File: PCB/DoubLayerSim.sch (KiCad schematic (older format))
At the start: 26 parts, among them J1 PanelSolar, J2 Bateria 3.7v, Q1 2N3904, U1 Moisture

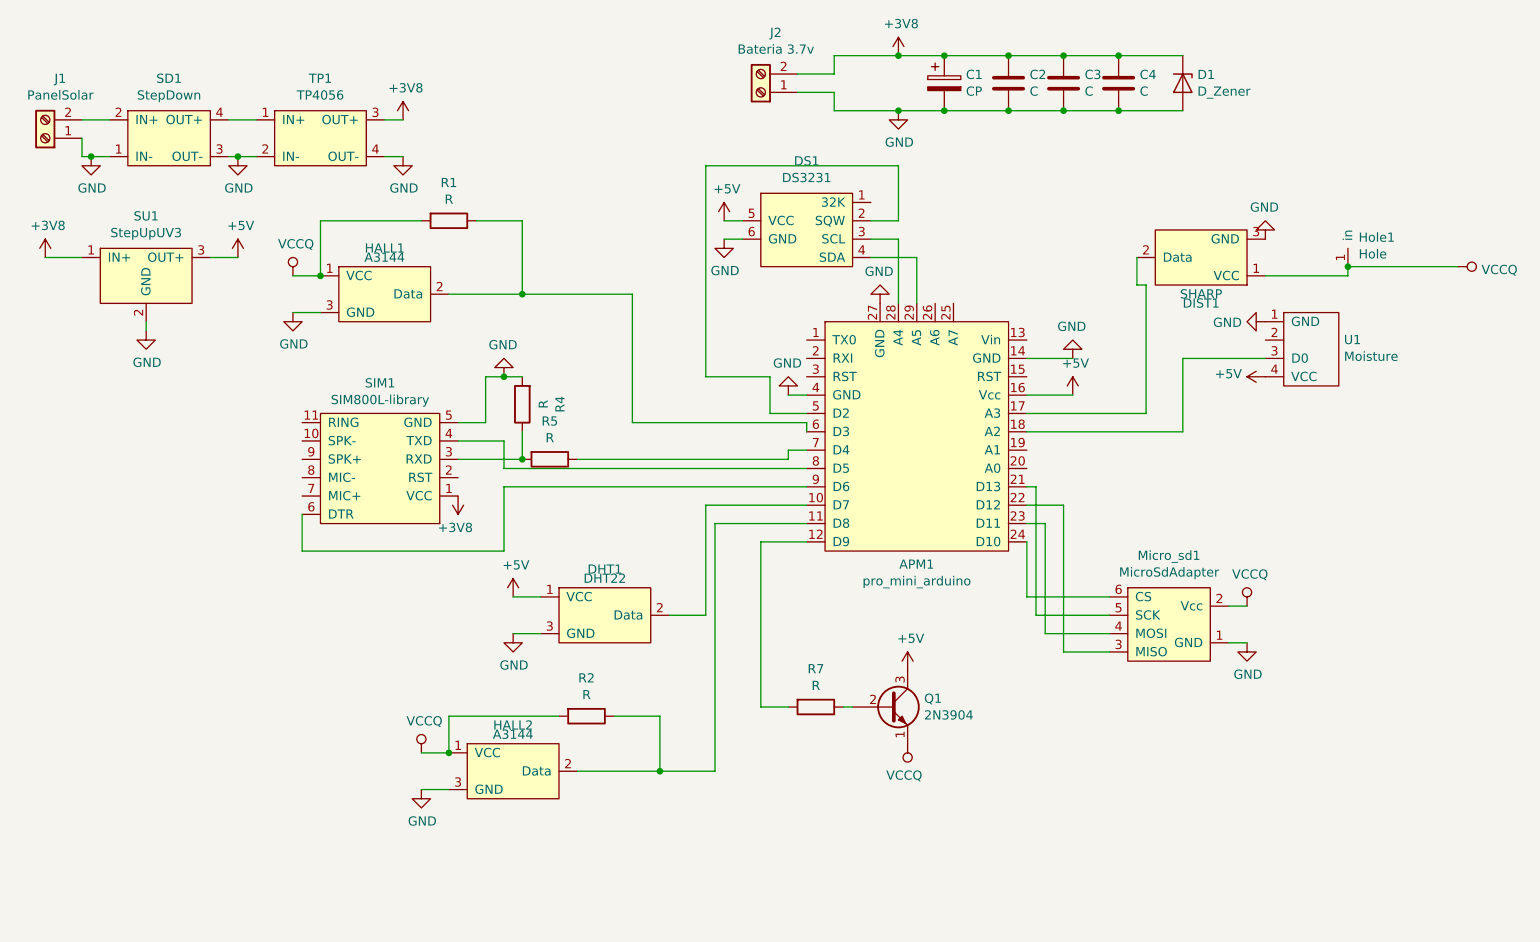
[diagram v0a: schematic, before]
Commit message: Cambio PCB Devolucion China
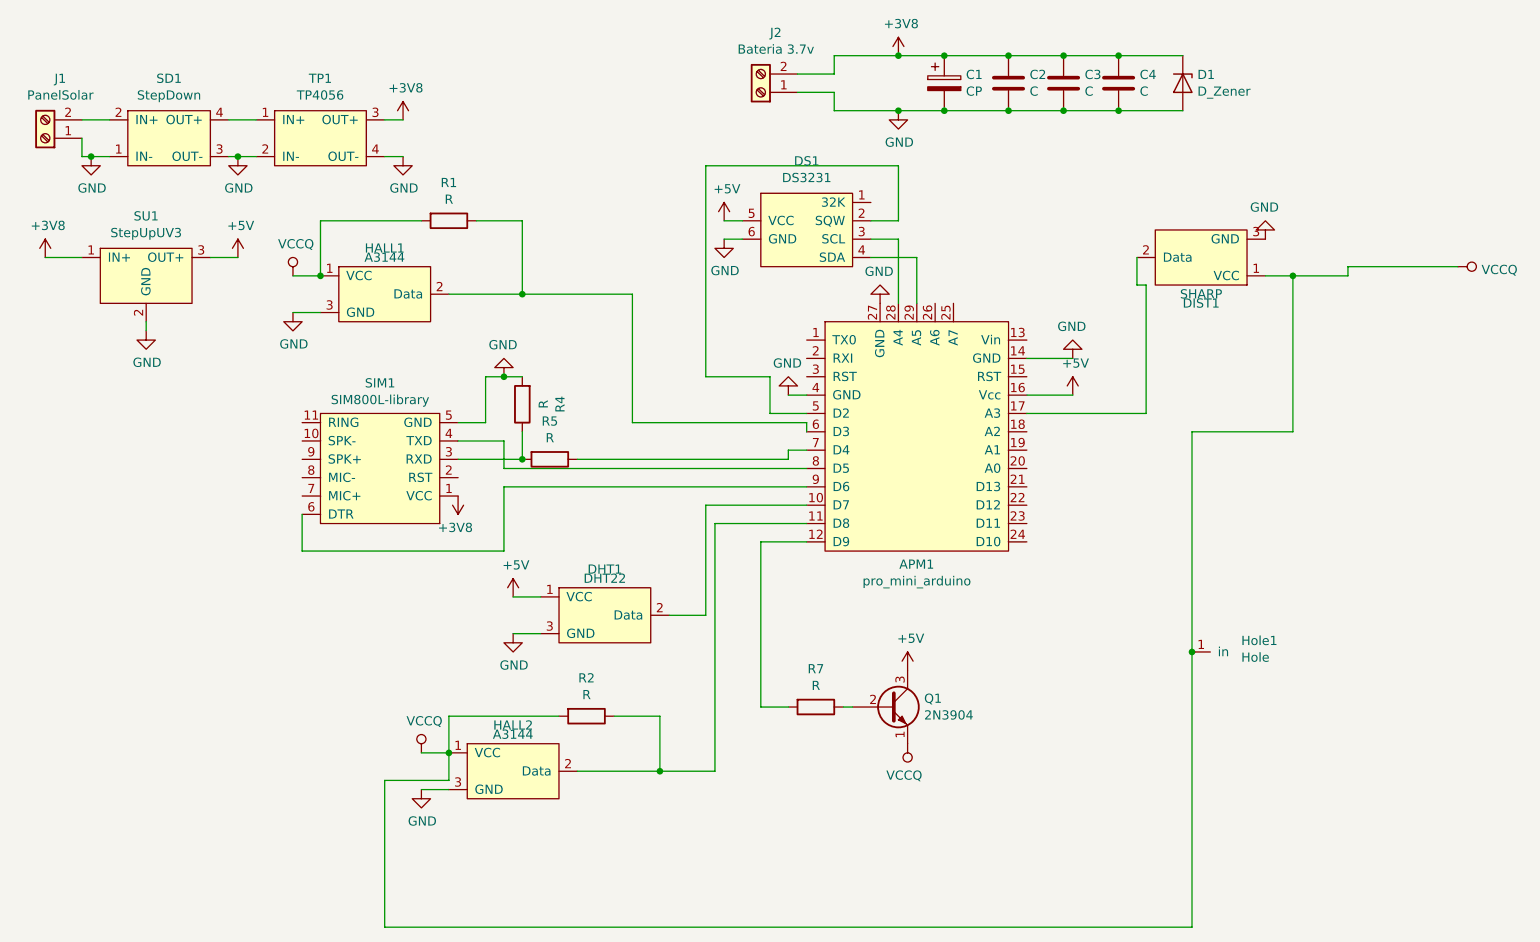
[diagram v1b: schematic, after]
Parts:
- removed Micro_sd1: MicroSdAdapter, pcb_ss:MicroSD_Adapter, symbol pcb-rescue:MicroSdAdapter-library
- removed U1: Moisture, pcb_ss:MOIS, symbol pcb-rescue:Moisture
- Hole1: footprint MountingHole:MountingHole_2.5mm_Pad -> MountingHole:MountingHole_2.2mm_M2_ISO7380_Pad
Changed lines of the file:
@@
 $EndDescr
-$Comp
-L pcb-rescue:DHT22-library DHT1
-U 1 1 5D9043F7
-P 4100 4150
-F 0 "DHT1" H 4100 4400 50  0000 C CNN
-F 1 "DHT22" H 4100 4350 50  0000 C CNN
-F 2 "pcb_ss:DHT22" H 4100 3850 50  0001 C CNN
-F 3 "" H 4100 3850 50  0001 C CNN
-	1    4100 4150
-	1    0    0    -1
-$EndComp
-$Comp
-L pcb-rescue:MicroSdAdapter-library Micro_sd1
-U 1 1 5D9081CE
-P 7200 4200
-F 0 "Micro_sd1" H 7175 4575 50  0000 C CNN
-F 1 "MicroSdAdapter" H 7175 4484 50  0000 C CNN
-F 2 "pcb_ss:MicroSD_Adapter" H 6650 3100 50  0001 C CNN
-F 3 "" H 6650 3100 50  0001 C CNN
-	1    7200 4200
-	1    0    0    -1
-$EndComp
 $Comp
 L Connector:Screw_Terminal_01x02 J2
@@
 Wire Wire Line
 	1600 2600 1600 2550
-$Comp
-L power:GND #PWR09
-U 1 1 5D92BDA7
-P 3600 4250
-F 0 "#PWR09" H 3600 4000 50  0001 C CNN
-F 1 "GND" H 3605 4077 50  0000 C CNN
-F 2 "" H 3600 4250 50  0001 C CNN
-F 3 "" H 3600 4250 50  0001 C CNN
-	1    3600 4250
-	1    0    0    -1
-$EndComp
-$Comp
-L power:GND #PWR019
-U 1 1 5D92C2D9
-P 7600 4300
-F 0 "#PWR019" H 7600 4050 50  0001 C CNN
-F 1 "GND" H 7605 4127 50  0000 C CNN
-F 2 "" H 7600 4300 50  0001 C CNN
-F 3 "" H 7600 4300 50  0001 C CNN
-	1    7600 4300
-	1    0    0    -1
-$EndComp
-Wire Wire Line
-	3750 4250 3600 4250
-Wire Wire Line
-	3750 4050 3600 4050
-Wire Wire Line
-	7500 4300 7600 4300
 Wire Wire Line
 	6400 2750 6650 2750
-Wire Wire Line
-	6850 4050 6400 4050
-Wire Wire Line
-	6400 4050 6400 3750
-Wire Wire Line
-	6850 4150 6450 4150
-Wire Wire Line
-	6450 4150 6450 3450
-Wire Wire Line
-	6450 3450 6400 3450
-Wire Wire Line
-	6850 4250 6500 4250
-Wire Wire Line
-	6500 4250 6500 3650
-Wire Wire Line
-	6500 3650 6400 3650
-Wire Wire Line
-	6850 4350 6600 4350
-Wire Wire Line
-	6600 3550 6400 3550
-Wire Wire Line
-	6600 3550 6600 4350
 Wire Wire Line
 	4750 2100 4850 2100
@@
 	1    0    0    -1
 $EndComp
-Wire Wire Line
-	7500 4100 7600 4100
 $Comp
 L power:+3V8 #PWR011
@@
 $EndComp
 Wire Wire Line
-	4450 4150 4650 4150
-Wire Wire Line
-	4650 3550 4650 4150
-Wire Wire Line
 	5350 1200 5350 1100
 Wire Wire Line
@@
 	5550 2100 5700 2100
 Wire Wire Line
-	4650 3550 5200 3550
-Wire Wire Line
 	5000 3050 5200 3050
 Wire Wire Line
@@
 Wire Wire Line
 	4250 2400 4250 3100
-Wire Wire Line
-	4250 3100 5200 3100
 Wire Wire Line
 	5200 3100 5200 3150
@@
 	3450 2850 3550 2850
 Wire Wire Line
-	3950 3300 5100 3300
-Wire Wire Line
 	5100 3300 5100 3250
 Wire Wire Line
@@
 Wire Wire Line
 	7050 2350 7000 2350
-$Comp
-L pcb-rescue:Moisture U1
-U 1 1 5E40ECC0
-P 7850 2650
-F 0 "U1" H 8128 2651 50  0000 L CNN
-F 1 "Moisture" H 8128 2560 50  0000 L CNN
-F 2 "pcb_ss:MOIS" H 7850 2650 50  0001 C CNN
-F 3 "" H 7850 2650 50  0001 C CNN
-	1    7850 2650
-	1    0    0    -1
-$EndComp
-Wire Wire Line
-	7700 2750 7250 2750
-Wire Wire Line
-	7250 2750 7250 3150
-Wire Wire Line
-	7250 3150 6400 3150
 Wire Wire Line
 	7000 2350 7000 2200
@@
 	1    7700 2100
 	-1   0    0    1
-$EndComp
-$Comp
-L power:GND #PWR0113
-U 1 1 5E422347
-P 7700 2550
-F 0 "#PWR0113" H 7700 2300 50  0001 C CNN
-F 1 "GND" V 7705 2422 50  0000 R CNN
-F 2 "" H 7700 2550 50  0001 C CNN
-F 3 "" H 7700 2550 50  0001 C CNN
-	1    7700 2550
-	0    1    1    0
-$EndComp
-$Comp
-L power:+5V #PWR0116
-U 1 1 5E424244
-P 7700 2850
-F 0 "#PWR0116" H 7700 2700 50  0001 C CNN
-F 1 "+5V" V 7715 2978 50  0000 L CNN
-F 2 "" H 7700 2850 50  0001 C CNN
-F 3 "" H 7700 2850 50  0001 C CNN
-	1    7700 2850
-	0    -1   -1   0
 $EndComp
 $Comp
@@
 $EndComp
 $Comp
-L power:VCCQ #PWR0114
-U 1 1 5E46AECC
-P 7600 4100
-F 0 "#PWR0114" H 7600 3950 50  0001 C CNN
-F 1 "VCCQ" H 7617 4273 50  0000 C CNN
-F 2 "" H 7600 4100 50  0001 C CNN
-F 3 "" H 7600 4100 50  0001 C CNN
-	1    7600 4100
-	1    0    0    -1
-$EndComp
-$Comp
 L power:VCCQ #PWR0104
 U 1 1 5E487CF9
@@
 $EndComp
 $Comp
+L power:VCCQ #PWR0106
+U 1 1 5E488F85
+P 3100 4900
+F 0 "#PWR0106" H 3100 4750 50  0001 C CNN
+F 1 "VCCQ" H 3117 5073 50  0000 C CNN
+F 2 "" H 3100 4900 50  0001 C CNN
+F 3 "" H 3100 4900 50  0001 C CNN
+	1    3100 4900
+	1    0    0    -1
+$EndComp
+$Comp
+L power:VCCQ #PWR0108
+U 1 1 5E489824
+P 2400 2300
+F 0 "#PWR0108" H 2400 2150 50  0001 C CNN
+F 1 "VCCQ" H 2417 2473 50  0000 C CNN
+F 2 "" H 2400 2300 50  0001 C CNN
+F 3 "" H 2400 2300 50  0001 C CNN
+	1    2400 2300
+	1    0    0    -1
+$EndComp
+Wire Wire Line
+	8150 2250 8750 2250
+Wire Wire Line
+	7700 2300 7850 2300
+Wire Wire Line
+	8150 2300 8150 2250
+Wire Wire Line
+	3950 3300 5100 3300
+Wire Wire Line
+	4250 3100 5200 3100
+$Comp
 L power:+5V #PWR012
 U 1 1 5DB484B5
@@
 	1    0    0    -1
 $EndComp
-$Comp
-L power:VCCQ #PWR0106
-U 1 1 5E488F85
-P 3100 4900
-F 0 "#PWR0106" H 3100 4750 50  0001 C CNN
-F 1 "VCCQ" H 3117 5073 50  0000 C CNN
-F 2 "" H 3100 4900 50  0001 C CNN
-F 3 "" H 3100 4900 50  0001 C CNN
-	1    3100 4900
-	1    0    0    -1
-$EndComp
-$Comp
-L power:VCCQ #PWR0108
-U 1 1 5E489824
-P 2400 2300
-F 0 "#PWR0108" H 2400 2150 50  0001 C CNN
-F 1 "VCCQ" H 2417 2473 50  0000 C CNN
-F 2 "" H 2400 2300 50  0001 C CNN
-F 3 "" H 2400 2300 50  0001 C CNN
-	1    2400 2300
-	1    0    0    -1
-$EndComp
+Wire Wire Line
+	4450 4150 4650 4150
+Wire Wire Line
+	3750 4050 3600 4050
+Wire Wire Line
+	3750 4250 3600 4250
+$Comp
+L power:GND #PWR09
+U 1 1 5D92BDA7
+P 3600 4250
+F 0 "#PWR09" H 3600 4000 50  0001 C CNN
+F 1 "GND" H 3605 4077 50  0000 C CNN
+F 2 "" H 3600 4250 50  0001 C CNN
+F 3 "" H 3600 4250 50  0001 C CNN
+	1    3600 4250
+	1    0    0    -1
+$EndComp
+$Comp
+L pcb-rescue:DHT22-library DHT1
+U 1 1 5D9043F7
+P 4100 4150
+F 0 "DHT1" H 4100 4400 50  0000 C CNN
+F 1 "DHT22" H 4100 4350 50  0000 C CNN
+F 2 "pcb_ss:DHT22" H 4100 3850 50  0001 C CNN
+F 3 "" H 4100 3850 50  0001 C CNN
+	1    4100 4150
+	1    0    0    -1
+$EndComp
+Wire Wire Line
+	4650 3550 4650 4150
+Wire Wire Line
+	4650 3550 5200 3550
 $Comp
 L pcb-rescue:Hole Hole1
-U 1 1 5E4B1FC3
-P 8150 2050
-F 0 "Hole1" V 8109 1992 50  0000 R CNN
-F 1 "Hole" V 8018 1992 50  0000 R CNN
-F 2 "MountingHole:MountingHole_2.5mm_Pad" H 8200 2050 50  0001 C CNN
-F 3 "" H 8200 2050 50  0001 C CNN
-	1    8150 2050
-	0    -1   -1   0
-$EndComp
-Wire Wire Line
-	8150 2250 8750 2250
-Wire Wire Line
-	7700 2300 8150 2300
-Wire Wire Line
-	8150 2300 8150 2250
-Connection ~ 8150 2250
+U 1 1 5E8A889E
+P 7500 4350
+F 0 "Hole1" H 7568 4411 50  0000 L CNN
+F 1 "Hole" H 7568 4320 50  0000 L CNN
+F 2 "MountingHole:MountingHole_2.2mm_M2_ISO7380_Pad" H 7550 4350 50  0001 C CNN
+F 3 "" H 7550 4350 50  0001 C CNN
+	1    7500 4350
+	1    0    0    -1
+$EndComp
+Wire Wire Line
+	3250 4900 3250 5050
+Wire Wire Line
+	3250 5050 2900 5050
+Wire Wire Line
+	2900 5050 2900 5850
+Wire Wire Line
+	2900 5850 7300 5850
+Wire Wire Line
+	7300 5850 7300 4350
+Wire Wire Line
+	7300 4350 7300 3150
+Wire Wire Line
+	7300 3150 7850 3150
+Wire Wire Line
+	7850 3150 7850 2300
+Connection ~ 7300 4350
+Connection ~ 7850 2300
+Wire Wire Line
+	7850 2300 8150 2300
 $EndSCHEMATC
